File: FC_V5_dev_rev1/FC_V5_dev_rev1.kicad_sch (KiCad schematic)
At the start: 80 parts, among them IC1 RP2040_QFN56, IC2 AZ1117CH-3.3TRG1, IC3 RV-3028-C7_32.768kHz_1ppm_TA_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, J1 Conn_ARM_JTAG_SWD_10, J11 Conn_Coaxial, J12 USB_C_Receptacle_USB2.0_16P, J16 DEBUG, J3 Life Makes Lemonade, J4 Molex 503398-1892, J5 BM04B-SRSS-TB(LF)(SN), J6 Conn_Coaxial, J9 BM04B-SRSS-TB(LF)(SN), SW1 KMR2, SW2 KMR2, SW3 SW_Push_SPDT, U12 TCA9548ARGERQ1, U16 MCP9808T-E/MS, U2 E22-400M30S, U4 RFM98PW, U5 RFM9xBreakout, U6 W25Q128JV, U7 LSM6DSOTR, U8 LSM303AGRTR, Y1 12MHZ

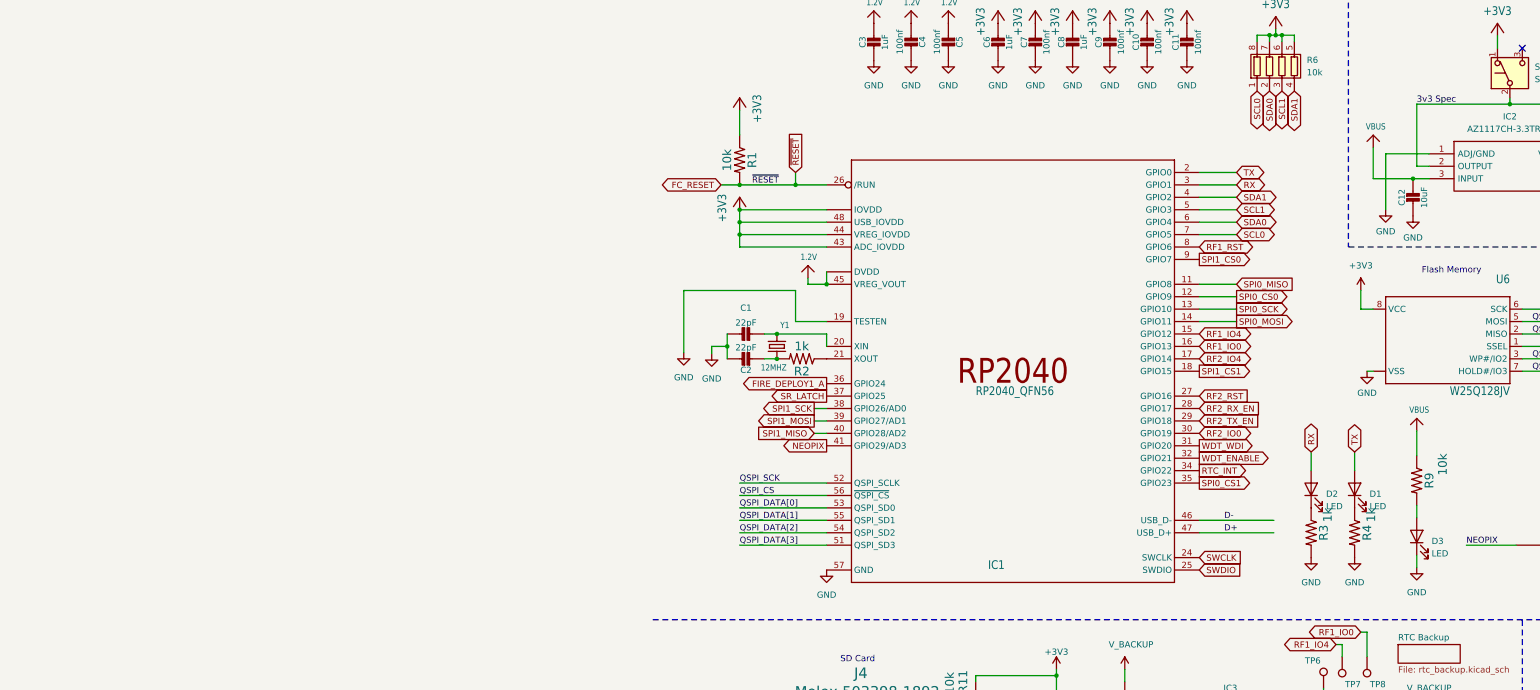
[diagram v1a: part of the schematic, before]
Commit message: Fixed Loadswitch Layouts
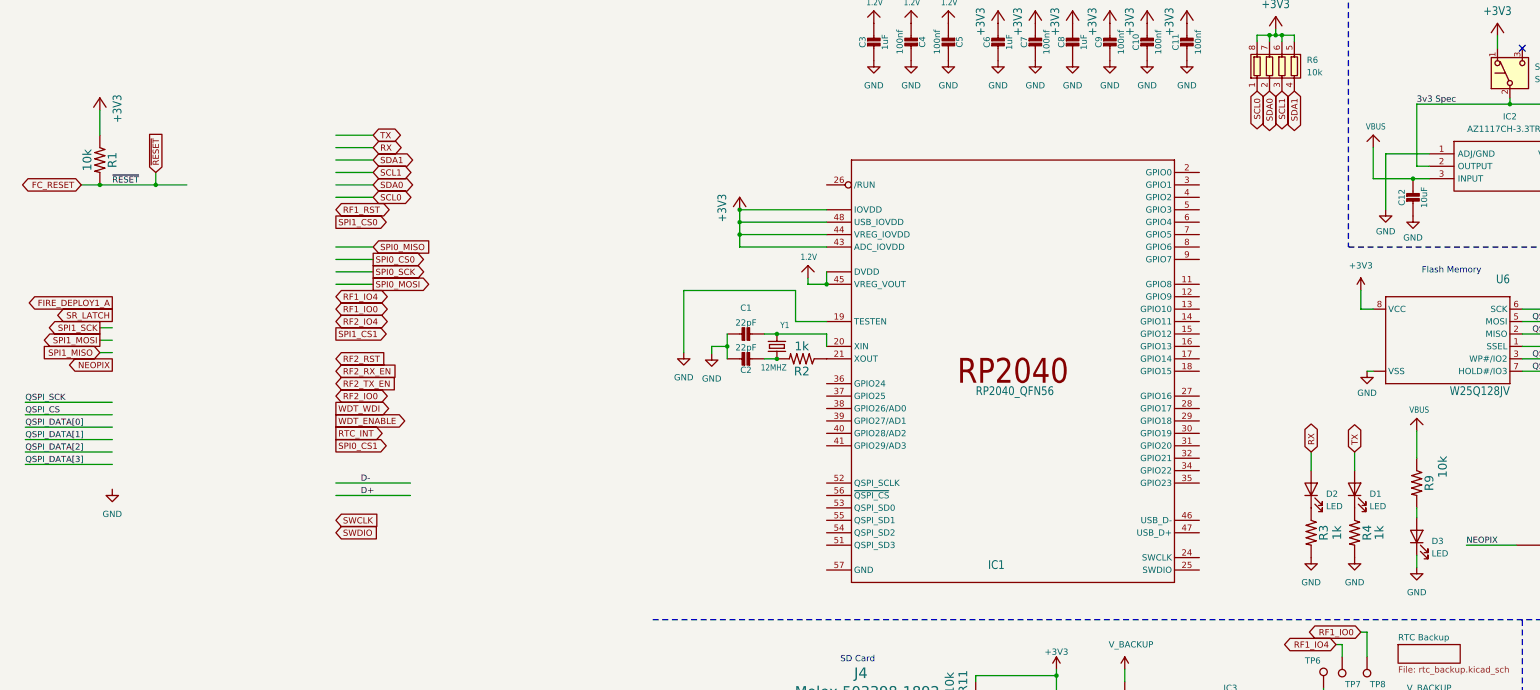
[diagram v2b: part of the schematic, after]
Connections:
- net D+: no longer IC1.47 (USB_D+)
- net D-: no longer IC1.46 (USB_D-)
- net FC_RESET: no longer IC1.26 (/RUN)
- net FIRE_DEPLOY1_A: no longer IC1.36 (GPIO24)
- net GND: no longer IC1.57 (GND)
- net NEOPIX: no longer IC1.41 (GPIO29/AD3)
- net QSPI_CS: no longer IC1.56 (~{QSPI_CS})
- net QSPI_DATA[0]: no longer IC1.53 (QSPI_SD0)
- net QSPI_DATA[1]: no longer IC1.55 (QSPI_SD1)
- net QSPI_DATA[2]: no longer IC1.54 (QSPI_SD2)
- net QSPI_DATA[3]: no longer IC1.51 (QSPI_SD3)
- net QSPI_SCK: no longer IC1.52 (QSPI_SCLK)
- net RF1_IO0: no longer IC1.16 (GPIO13)
- net RF1_IO4: no longer IC1.15 (GPIO12)
- net RF1_RST: no longer IC1.8 (GPIO6)
- net RF2_IO0: no longer IC1.30 (GPIO19)
- net RF2_IO4: no longer IC1.17 (GPIO14)
- net RF2_RST: no longer IC1.27 (GPIO16)
- net RF2_RX_EN: no longer IC1.28 (GPIO17)
- net RF2_TX_EN: no longer IC1.29 (GPIO18)
- net RTC_INT: no longer IC1.34 (GPIO22)
- net RX: no longer IC1.3 (GPIO1)
- net SCL0: no longer IC1.7 (GPIO5)
- net SCL1: no longer IC1.5 (GPIO3)
- net SDA0: no longer IC1.6 (GPIO4)
- net SDA1: no longer IC1.4 (GPIO2)
- net SPI0_CS0: no longer IC1.12 (GPIO9)
- net SPI0_CS1: no longer IC1.35 (GPIO23)
- net SPI0_MISO: no longer IC1.11 (GPIO8)
- net SPI0_MOSI: no longer IC1.14 (GPIO11)
- net SPI0_SCK: no longer IC1.13 (GPIO10)
- net SPI1_CS0: no longer IC1.9 (GPIO7)
- net SPI1_CS1: no longer IC1.18 (GPIO15)
- net SPI1_MISO: no longer IC1.40 (GPIO28/AD2)
- net SPI1_MOSI: no longer IC1.39 (GPIO27/AD1)
- net SPI1_SCK: no longer IC1.38 (GPIO26/AD0)
- net SR_LATCH: no longer IC1.37 (GPIO25)
- net SWCLK: no longer IC1.24 (SWCLK)
- net SWDIO: no longer IC1.25 (SWDIO)
- net TX: no longer IC1.2 (GPIO0)
- net WDT_ENABLE: no longer IC1.32 (GPIO21)
- net WDT_WDI: no longer IC1.31 (GPIO20)
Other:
- moved on the sheet: R1, R9

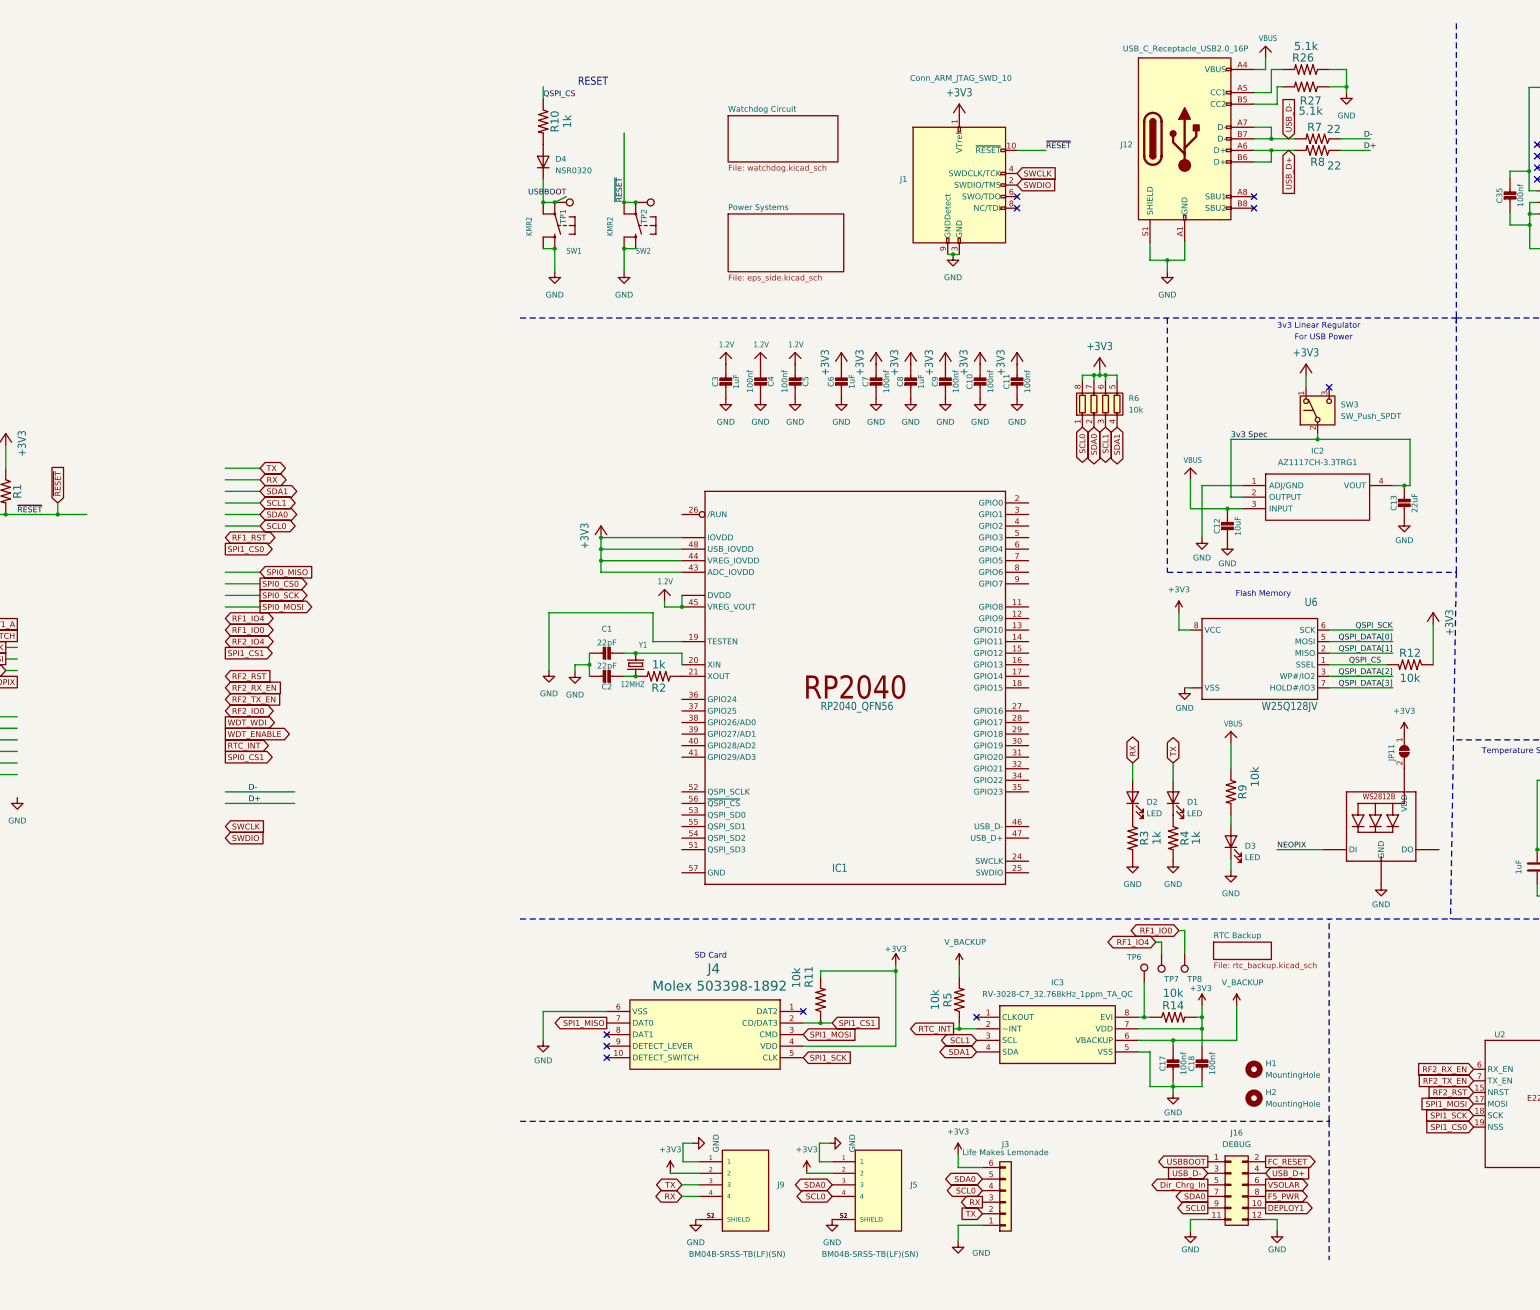
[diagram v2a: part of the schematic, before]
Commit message: Initial Creation of RP2350 Symbol
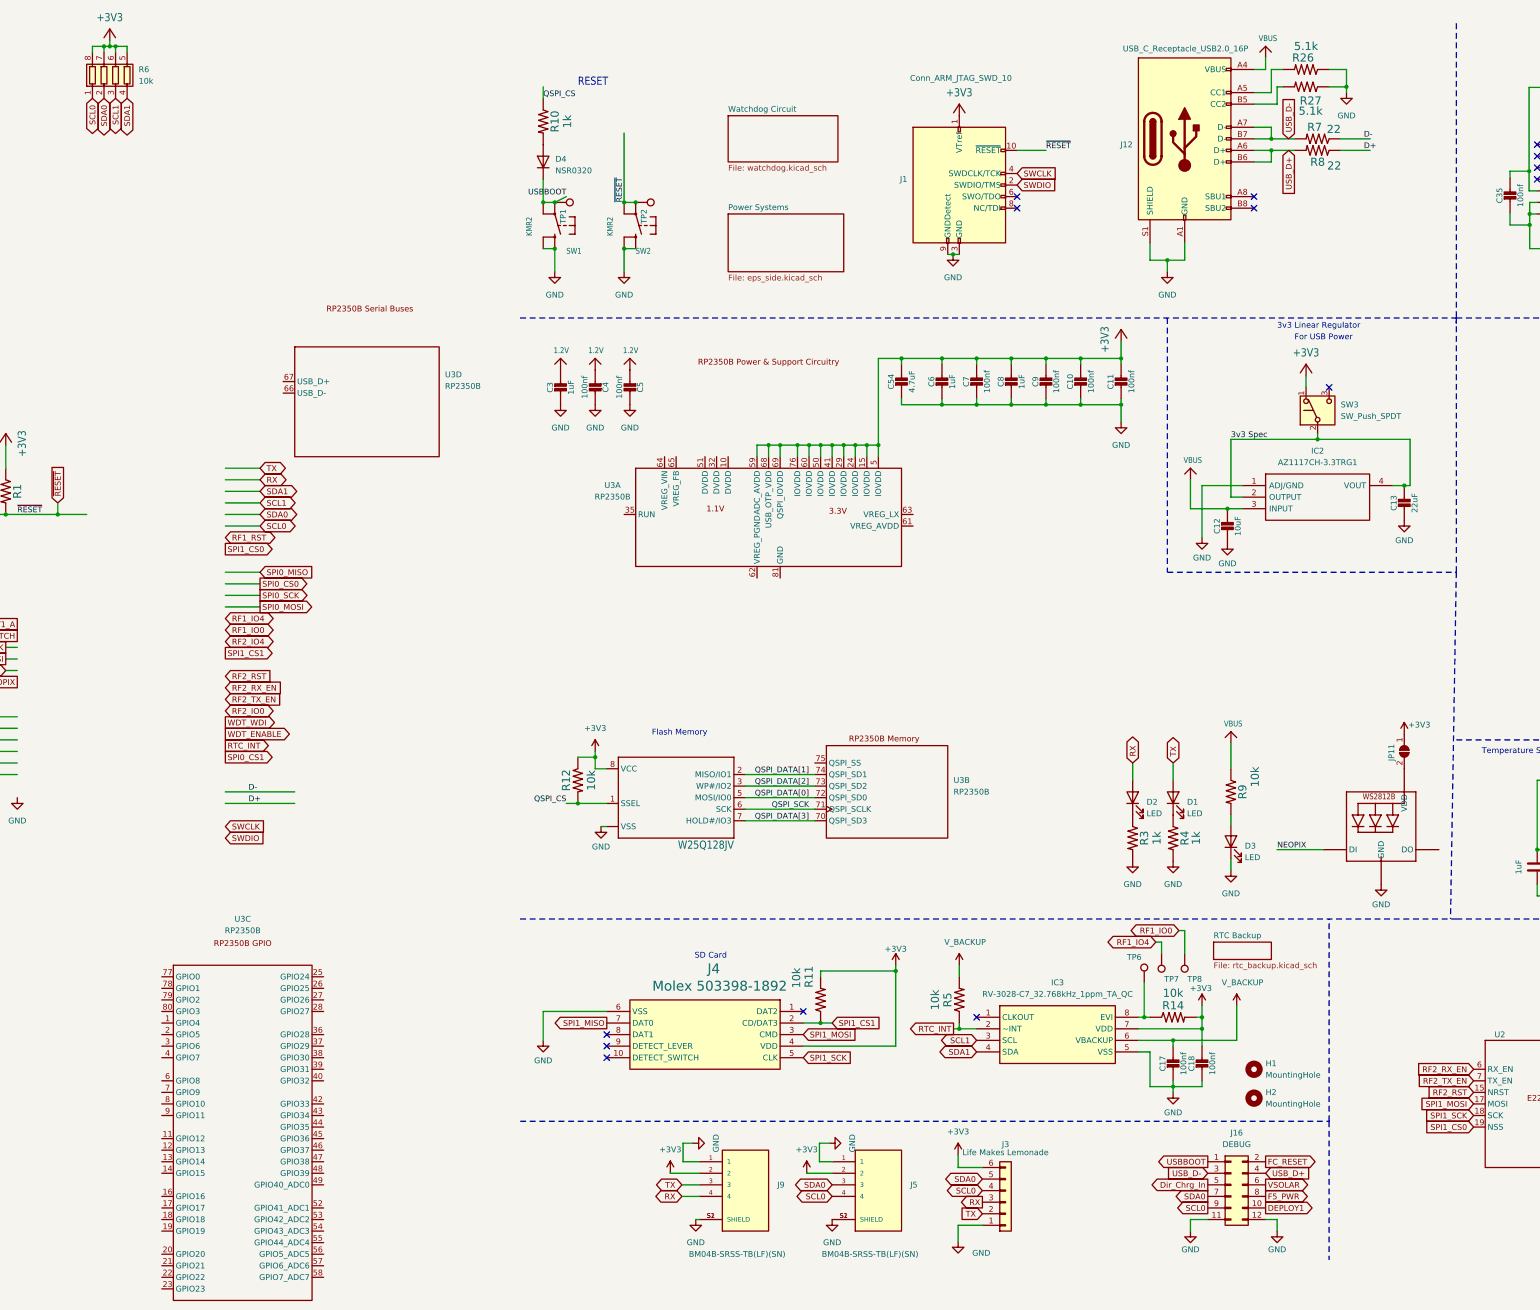
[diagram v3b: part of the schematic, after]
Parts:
- removed C1, C2: 22pF, Capacitor_SMD:C_0402_1005Metric, symbol Adafruit ItsyBitsy RP2040-eagle-import:CAP_CERAMIC_0402NO
- removed IC1: RP2040_QFN56, Package_DFN_QFN:QFN-56-1EP_7x7mm_P0.4mm_EP3.2x3.2mm_ThermalVias, symbol Adafruit ItsyBitsy RP2040-eagle-import:RP2040_QFN56
- removed R2: 1k, Resistor_SMD:R_0402_1005Metric, symbol mainboard:RESISTOR0603
- removed Y1: 12MHZ, Crystal:Crystal_SMD_2520-4Pin_2.5x2.0mm, symbol Adafruit ItsyBitsy RP2040-eagle-import:CRYSTAL2.5X2.0
- added C54: 4.7uF, Capacitor_SMD:C_0402_1005Metric, symbol Adafruit ItsyBitsy RP2040-eagle-import:CAP_CERAMIC_0603MP
- added U3: RP2350B, RP2350:QFN-80_L10.0-W10.0-P0.40-TL-EP3.4, symbol PROVES:RP2350B
- C6, C8: footprint Capacitor_SMD:C_0603_1608Metric -> Capacitor_SMD:C_0402_1005Metric
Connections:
- net +3V3: now also C54.1, U3.15 (IOVDD), U3.24 (IOVDD), U3.29 (IOVDD), U3.41 (IOVDD), U3.5 (IOVDD), U3.50 (IOVDD), U3.59 (ADC_AVDD), U3.60 (IOVDD), U3.68 (USB_OTP_VDD), U3.69 (QSPI_IOVDD), U3.76 (IOVDD)
- net GND: now also C54.2
- net QSPI_DATA[0]: now also U3.72 (QSPI_SD0)
- net QSPI_DATA[1]: now also U3.74 (QSPI_SD1)
- net QSPI_DATA[2]: now also U3.73 (QSPI_SD2)
- net QSPI_DATA[3]: now also U3.70 (QSPI_SD3)
- net QSPI_SCK: now also U3.71 (QSPI_SCLK)
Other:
- moved on the sheet: C10, C11, C3, C4, C5, C6, C7, C8, C9, R12, R6

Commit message: Incremental Layout Work
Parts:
- added C56, C57, C58: 4.7uF, Capacitor_SMD:C_0402_1005Metric, symbol Adafruit ItsyBitsy RP2040-eagle-import:CAP_CERAMIC_0603MP
- added L3: L, symbol Device:L
- added R24: 33, Resistor_SMD:R_0603_1608Metric, symbol mainboard:RESISTOR0603
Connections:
- net +3V3: now also U3.64 (VREG_VIN), C57.1, R24.2
- net 1.2V: now also U3.10 (DVDD), U3.32 (DVDD), U3.51 (DVDD)
- net D+: now also U3.67 (USB_D+)
- net D-: now also U3.66 (USB_D-)
- net FC_RESET: now also U3.35 (RUN)
- net GND: now also U3.62 (VREG_PGND), U3.81 (GND), C56.2, C57.2, C58.2
- net SWCLK: now also U3.24 (SWCLK)
- net SWDIO: now also U3.25 (SWDIO)
- net at U3.61 (VREG_AVDD): now also C58.1, R24.1
- net VREG_LX: now reaches U3.63 (VREG_LX)
- net VREG_LX: now also L3.2
- net +1V1: now reaches U3.65 (VREG_FB)
- net +1V1: now also C56.1, L3.1
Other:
- moved on the sheet: C10, C11, C12, C13, C3, C4, C5, C54, C6, C7, C8, C9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
